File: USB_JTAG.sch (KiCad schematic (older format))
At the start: 29 parts, among them J4 USB_B_Micro, J5 AVR-JTAG-10, U10 FT2232H, U11 5M1270ZT144C5N, U12 93LCxxBxxOT, U9 TPD2EUSB30

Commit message: Updated BOM
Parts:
- removed U10: FT2232H, Package_QFP:LQFP-64_10x10mm_P0.5mm, symbol Interface_USB:FT2232H
- added U8: FT2232H, Package_QFP:TQFP-64_10x10mm_P0.5mm, symbol Interface_USB:FT2232H
- C16, C18: MFR KEMET -> Taiyo Yuden; MPN C0805C104K4RACTU -> JMK107BB7475KA-T; SPN 80-C0805C104K4R -> (none)
- C17, C19, C23, C24, C25, C26, C27, C28, C29, C30: MFR KEMET -> Taiyo Yuden; MPN C0805C104K4RACTU -> TMK107BJ104KA-T; SPN 80-C0805C104K4R -> (none)
- D1: MFR (none) -> Lite-On; MPN (none) -> LTST-C190KGKT; SPR (none) -> Mouser
- L1, L2: MFR (none) -> TDK; MPN (none) -> MMZ1608R601ATA00; SPR (none) -> Mouser
- R5: MFR (none) -> Yageo; MPN (none) -> RC0603JR-0712KL; SPR (none) -> Mouser
- R6: MFR (none) -> Yageo; MPN (none) -> RC0603JR-071KL; SPR (none) -> Mouser
- R7: MFR (none) -> Yageo; MPN (none) -> RC0603JR-071ML; SPR (none) -> Mouser
- R8: MFR (none) -> Yageo; MPN (none) -> RC0603JR-07220RL; SPR (none) -> Mouser
- R9: MFR (none) -> Yageo; MPN (none) -> RC0603JR-072K2L; SPR (none) -> Mouser
- RN2: MFR (none) -> Panasonic; MPN (none) -> EXB-38V220JV; SPR (none) -> Mouser
- RN3, RN4: MFR (none) -> Panasonic; MPN (none) -> EXB-38V103JV; SPR (none) -> Mouser
- U11: MFR (none) -> Intel; MPN (none) -> 5M1270ZT144C5N; Manufacturer_Name Intel -> (none); SPR (none) -> Mouser
- U12: value 93LCxxBxxOT -> 93LC46BT-I/OT; MFR (none) -> Microchip; MPN (none) -> 93LC46BT-I/OT; SPR (none) -> Mouser
- U9: MFR (none) -> Texas Instruments; MPN (none) -> TPD2EUSB30DRTR; SPR (none) -> Mouser
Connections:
- wire segments 141 -> 142
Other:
- moved on the sheet: D1, R8

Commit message: updated descriptions and part #'s
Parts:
- C16, C18: Description (none) -> Multilayer Ceramic Capacitors MLCC - SMD/SMT 4.7uF 6.3V X7R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; SPN (none) -> 963-JMK107BB7475KA-T; SPURL https://www.mouser.com/ProductDetail/KEMET/C0805C104K4RACTU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 -> https://www.mouser.com/ProductDetail/963-JMK107BB7475KA-T
- C17, C19, C23, C24, C25, C26, C27, C28, C29, C30: Description (none) -> Multilayer Ceramic Capacitors MLCC - SMD/SMT 0.1uF 25V X5R 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; SPN (none) -> 963-TMK107BJ104KA-T; SPURL https://www.mouser.com/ProductDetail/KEMET/C0805C104K4RACTU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 -> https://www.mouser.com/ProductDetail/963-TMK107BJ104KA-T
- D1: Description (none) -> Standard LEDs - SMD Green Clear 571nm; SPN (none) -> 859-LTST-C190KGKT; SPURL (none) -> https://www.mouser.com/ProductDetail/859-LTST-C190KGKT
- L1, L2: Description (none) -> Ferrite Beads 600 OHM 25%; SPN (none) -> 810-MMZ1608R601ATA00; SPURL (none) -> https://www.mouser.com/ProductDetail/810-MMZ1608R601ATA00
- R5: Description (none) -> Thick Film Resistors - SMD 12K OHM 5%; SPN (none) -> 603-RC0603JR-0712KL; SPURL (none) -> https://www.mouser.com/ProductDetail/603-RC0603JR-0712KL
- R6: Description (none) -> Thick Film Resistors - SMD 1K OHM 5%; SPN (none) -> 603-RC0603JR-071KL; SPURL (none) -> https://www.mouser.com/ProductDetail/603-RC0603JR-071KL
- R7: Description (none) -> Thick Film Resistors - SMD 1M OHM 5%; SPN (none) -> 603-RC0603JR-071ML; SPURL (none) -> https://www.mouser.com/ProductDetail/603-RC0603JR-071ML
- R8: Description (none) -> Thick Film Resistors - SMD 220 OHM 5%; SPN (none) -> 603-RC0603JR-07220RL; SPURL (none) -> https://www.mouser.com/ProductDetail/603-RC0603JR-07220RL
- R9: Description (none) -> Thick Film Resistors - SMD 2.2K OHM 5%; SPN (none) -> 603-RC0603JR-072K2L; SPURL (none) -> https://www.mouser.com/ProductDetail/603-RC0603JR-072K2L
- RN2: Description (none) -> Resistor Networks & Arrays 22 OHM 5%; SPN (none) -> 667-EXB-38V220JV; SPURL (none) -> https://www.mouser.com/ProductDetail/667-EXB-38V220JV
- RN3, RN4: Description (none) -> Resistor Networks & Arrays 10K OHM 5%; SPN (none) -> 667-EXB-38V103JV; SPURL (none) -> https://www.mouser.com/ProductDetail/667-EXB-38V103JV
- U11: SPN (none) -> 989-5M1270ZT144C5N; SPURL (none) -> https://www.mouser.com/ProductDetail/989-5M1270ZT144C5N
- U12: Description (none) -> EEPROM 64x16; SPN (none) -> 579-93LC46BT-I/OT; SPURL (none) -> https://www.mouser.com/ProductDetail/579-93LC46BT-I/OT
- U8: symbol Interface_USB:FT2232H -> rc2014_max_v-rescue:FT2232H-Interface_USB; Description (none) -> USB Interface IC USB HS to Dual UART/ FIFO/SPI/JTAG/I2C; SPN (none) -> 895-FT2232HL; SPURL (none) -> https://www.mouser.com/ProductDetail/895-FT2232HL
- U9: Description (none) -> ESD Suppressors / TVS Diodes 2Ch ESD Solution; SPN (none) -> 595-TPD2EUSB30DRTR; SPURL (none) -> https://www.mouser.com/ProductDetail/595-TPD2EUSB30DRTR

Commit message: mirror flipped the chips
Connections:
- net JTAG_TDO: now also RN3.2 (R2.1); no longer RN3.3 (R3.1)
- net JTAG_TMS: now also RN3.3 (R3.1); no longer RN3.2 (R2.1)
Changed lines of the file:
@@
 	7930 2430 8060 2430
 Wire Wire Line
-	9890 3780 10300 3780
-Wire Wire Line
 	10450 3780 10450 3790
 Wire Wire Line
-	9890 3680 10200 3680
-Wire Wire Line
 	10450 3680 10450 3690
-Wire Wire Line
-	9890 3580 10100 3580
-Wire Wire Line
-	9890 3480 10000 3480
-Wire Wire Line
-	10000 3000 10000 3480
-Wire Wire Line
-	10000 3480 10450 3480
-Wire Wire Line
-	10100 3000 10100 3580
-Wire Wire Line
-	10100 3580 10450 3580
-Wire Wire Line
-	10200 3000 10200 3680
-Wire Wire Line
-	10200 3680 10450 3680
-Wire Wire Line
-	10300 3000 10300 3780
-Wire Wire Line
-	10300 3780 10450 3780
 Wire Wire Line
 	10300 2600 10300 2610
@@
 Connection ~ 1640 6910
 Connection ~ 1640 7210
-Connection ~ 10000 3480
-Connection ~ 10100 3580
-Connection ~ 10200 3680
-Connection ~ 10300 3780
 Connection ~ 6550 1830
 Connection ~ 3480 3830
@@
 NoConn ~ 7400 5330
 NoConn ~ 5000 5630
+Wire Wire Line
+	9890 3680 10100 3680
+Wire Wire Line
+	9890 3580 10200 3580
+Wire Wire Line
+	10200 3000 10200 3580
+Connection ~ 10200 3580
+Wire Wire Line
+	10200 3580 10450 3580
+Wire Wire Line
+	10100 3000 10100 3680
+Connection ~ 10100 3680
+Wire Wire Line
+	10100 3680 10450 3680
+Wire Wire Line
+	9890 3780 10300 3780
+Wire Wire Line
+	9890 3480 10000 3480
+Wire Wire Line
+	10000 3000 10000 3480
+Connection ~ 10000 3480
+Wire Wire Line
+	10000 3480 10450 3480
+Wire Wire Line
+	10300 3000 10300 3780
+Connection ~ 10300 3780
+Wire Wire Line
+	10300 3780 10450 3780
 $EndSCHEMATC

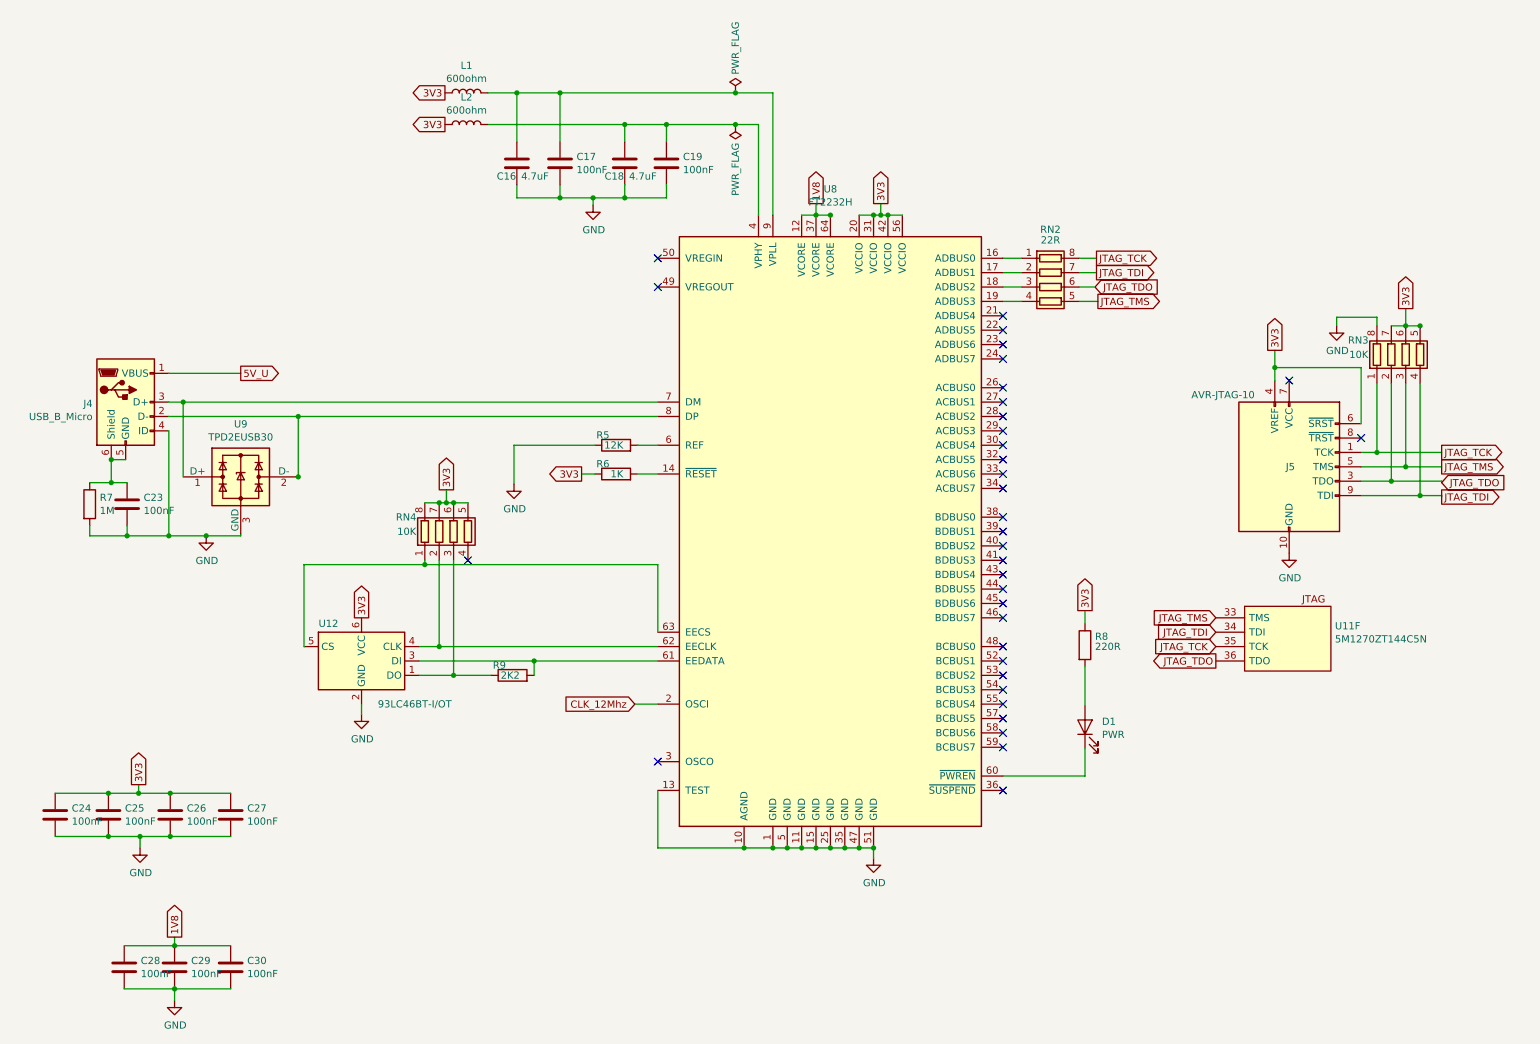
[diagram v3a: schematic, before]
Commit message: moved things around to improve routing, fixed power plane
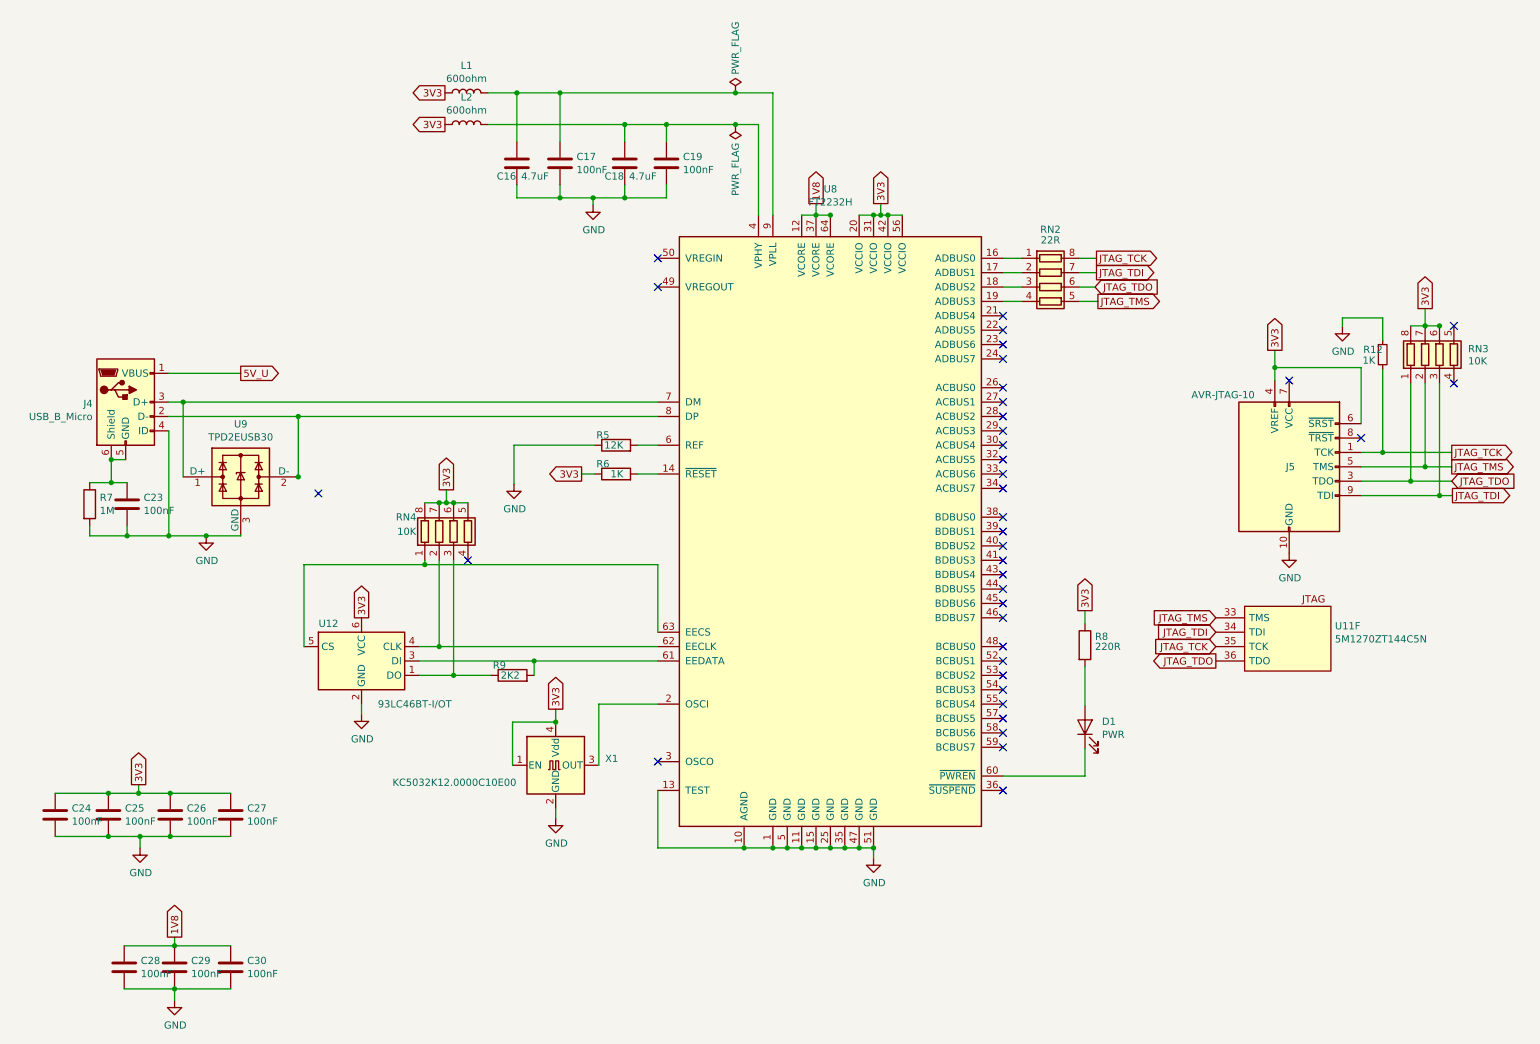
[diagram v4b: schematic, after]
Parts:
- added R12: 1K, Resistor_SMD:R_0603_1608Metric_Pad1.05x0.95mm_HandSolder, symbol Device:R_Small
- added X1: KC5032K12.0000C10E00, Oscillator:Oscillator_SMD_Fordahl_DFAS15-4Pin_5.0x3.2mm_HandSoldering, symbol Oscillator:KC5032K12.0000C10E00
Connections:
- net 3V3: now also RN3.8 (R1.2), X1.1 (EN), X1.4 (Vdd); no longer RN3.5 (R4.2)
- net GND: now also R12.1, X1.2 (GND); no longer RN3.8 (R1.2)
- net JTAG_TCK: now also R12.2; no longer RN3.1 (R1.1)
- net JTAG_TDI: now also RN3.3 (R3.1); no longer RN3.4 (R4.1)
- net JTAG_TDO: now also RN3.1 (R1.1); no longer RN3.2 (R2.1)
- net JTAG_TMS: now also RN3.2 (R2.1); no longer RN3.3 (R3.1)
- net CLK_12Mhz: no longer names the net of U8.2 (OSCI)
- net CLK_12Mhz: now also X1.3 (OUT)
- no-connect marks 35 -> 38
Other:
- moved on the sheet: RN3
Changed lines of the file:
@@
-$EndComp
-$Comp
-L Device:R_Pack04 RN3
-U 1 1 5CF8ACD2
-P 10200 2800
-AR Path="/5D0F9837/5CF8ACD2" Ref="RN3"  Part="1"
-AR Path="/5CF8ACD2" Ref="RN?"  Part="1"
-AR Path="/5CFABACD/5CF8ACD2" Ref="RN?"  Part="1"
-F 0 "RN3" H 9870 2900 50  0000 C CNN
-F 1 "10K" H 9874 2800 50  0000 C CNN
-F 2 "Resistor_SMD:R_Array_Concave_4x0603" V 10475 2800 50  0001 C CNN
-F 3 "https://www.mouser.com/datasheet/2/315/AOC0000C14-1108062.pdf" H 10200 2800 50  0001 C CNN
-F 4 "Resistor Networks & Arrays 10K OHM 5%" H 9870 3000 50  0001 C CNN "Description"
-F 5 "Panasonic" H 10200 2800 50  0001 C CNN "MFR"
-F 6 "EXB-38V103JV" H 10200 2800 50  0001 C CNN "MPN"
-F 7 "667-EXB-38V103JV" H 9870 3000 50  0001 C CNN "SPN"
-F 8 "Mouser" H 10200 2800 50  0001 C CNN "SPR"
-F 9 "https://www.mouser.com/ProductDetail/667-EXB-38V103JV" H 9870 3000 50  0001 C CNN "SPURL"
-	1    10200 2800
-	1    0    0    -1
 $EndComp
 $Comp
 L power:GND #PWR?
 U 1 1 5D1A4182
-P 9720 2600
+P 9760 2605
 AR Path="/5D1A4182" Ref="#PWR?"  Part="1"
 AR Path="/5CB63856/5D1A4182" Ref="#PWR?"  Part="1"
@@
 AR Path="/5CFABACD/5D1A4182" Ref="#PWR?"  Part="1"
 AR Path="/5D0F9837/5D1A4182" Ref="#PWR041"  Part="1"
-F 0 "#PWR041" H 9720 2350 50  0001 C CNN
-F 1 "GND" H 9725 2427 50  0000 C CNN
-F 2 "" H 9720 2600 50  0001 C CNN
-F 3 "" H 9720 2600 50  0001 C CNN
-	1    9720 2600
+F 0 "#PWR041" H 9760 2355 50  0001 C CNN
+F 1 "GND" H 9765 2432 50  0000 C CNN
+F 2 "" H 9760 2605 50  0001 C CNN
+F 3 "" H 9760 2605 50  0001 C CNN
+	1    9760 2605
 	1    0    0    -1
 $EndComp
@@
 Text GLabel 8060 2430 2    50   Output ~ 0
 JTAG_TMS
-Text GLabel 10450 3790 2    50   Output ~ 0
+Text GLabel 10525 3780 2    50   Output ~ 0
 JTAG_TDI
-Text GLabel 10450 3690 2    50   Input ~ 0
+Text GLabel 10520 3680 2    50   Input ~ 0
 JTAG_TDO
-Text GLabel 10450 3580 2    50   Output ~ 0
+Text GLabel 10520 3580 2    50   Output ~ 0
 JTAG_TMS
-Text GLabel 10450 3480 2    50   Output ~ 0
+Text GLabel 10520 3480 2    50   Output ~ 0
 JTAG_TCK
 Text GLabel 8880 4730 0    50   Input ~ 0
@@
 Text GLabel 8880 4830 0    50   Input ~ 0
 JTAG_TCK
-Text GLabel 4840 5230 0    50   Input ~ 0
-CLK_12Mhz
 Text GLabel 2100 2930 2    50   Output ~ 0
 5V_U
@@
 Text GLabel 3530 3740 1    50   Output ~ 0
 3V3
-Text GLabel 10200 2480 1    50   Output ~ 0
+Text GLabel 10335 2480 1    50   Output ~ 0
 3V3
 Text GLabel 9290 2770 1    50   Output ~ 0
@@
 	7930 2430 8060 2430
 Wire Wire Line
-	10450 3780 10450 3790
-Wire Wire Line
-	10450 3680 10450 3690
-Wire Wire Line
-	10300 2600 10300 2610
-Wire Wire Line
-	10200 2480 10200 2600
+	10435 2600 10435 2610
+Wire Wire Line
+	10335 2480 10335 2600
 Wire Wire Line
 	3380 3830 3480 3830
@@
 	3530 3830 3580 3830
 Wire Wire Line
-	10200 2600 10300 2600
-Wire Wire Line
-	10100 2600 10200 2600
-Wire Wire Line
-	10000 2600 10000 2540
-Wire Wire Line
-	10000 2540 9720 2540
-Wire Wire Line
-	9720 2540 9720 2600
+	10335 2600 10435 2600
+Wire Wire Line
+	10235 2600 10335 2600
+Wire Wire Line
+	10040 2545 9760 2545
+Wire Wire Line
+	9760 2545 9760 2605
 Wire Wire Line
 	9890 3280 9890 2890
@@
 Wire Wire Line
 	1640 7210 2030 7210
-Wire Wire Line
-	4840 5230 5000 5230
 Wire Wire Line
 	7400 5730 7970 5730
@@
 Connection ~ 3580 3830
 Connection ~ 3530 3830
-Connection ~ 10200 2600
-Connection ~ 10300 2600
+Connection ~ 10335 2600
 Connection ~ 9290 2890
 Connection ~ 1400 6150
@@
 NoConn ~ 7400 5330
 NoConn ~ 5000 5630
-Wire Wire Line
-	9890 3680 10100 3680
-Wire Wire Line
-	9890 3580 10200 3580
-Wire Wire Line
-	10200 3000 10200 3580
-Connection ~ 10200 3580
-Wire Wire Line
-	10200 3580 10450 3580
-Wire Wire Line
-	10100 3000 10100 3680
-Connection ~ 10100 3680
-Wire Wire Line
-	10100 3680 10450 3680
-Wire Wire Line
-	9890 3780 10300 3780
-Wire Wire Line
-	9890 3480 10000 3480
-Wire Wire Line
-	10000 3000 10000 3480
-Connection ~ 10000 3480
-Wire Wire Line
-	10000 3480 10450 3480
-Wire Wire Line
-	10300 3000 10300 3780
-Connection ~ 10300 3780
-Wire Wire Line
-	10300 3780 10450 3780
+$Comp
+L Oscillator:KC5032K12.0000C10E00 X1
+U 1 1 5D18454F
+P 4290 5655
+F 0 "X1" H 4634 5701 50  0000 L CNN
+F 1 "KC5032K12.0000C10E00" H 3155 5535 50  0000 L CNN
+F 2 "Oscillator:Oscillator_SMD_Fordahl_DFAS15-4Pin_5.0x3.2mm_HandSoldering" H 4990 5305 50  0001 C CNN
+F 3 "http://www.abracon.com/Oscillators/ASV.pdf" H 4190 5655 50  0001 C CNN
+	1    4290 5655
+	1    0    0    -1
+$EndComp
+Wire Wire Line
+	4590 5655 4590 5230
+Wire Wire Line
+	4590 5230 5000 5230
+Wire Wire Line
+	3990 5655 3990 5355
+Wire Wire Line
+	3990 5355 4290 5355
+Text GLabel 4290 5265 1    50   Output ~ 0
+3V3
+Wire Wire Line
+	4290 5265 4290 5355
+Connection ~ 4290 5355
+$Comp
+L power:GND #PWR02
+U 1 1 5D1A3145
+P 4290 6025
+F 0 "#PWR02" H 4290 5775 50  0001 C CNN
+F 1 "GND" H 4295 5852 50  0000 C CNN
+F 2 "" H 4290 6025 50  0001 C CNN
+F 3 "" H 4290 6025 50  0001 C CNN
+	1    4290 6025
+	1    0    0    -1
+$EndComp
+Wire Wire Line
+	4290 5955 4290 6025
+NoConn ~ 2640 3765
+Connection ~ 10435 2600
+Wire Wire Line
+	10435 3000 10435 3780
+$Comp
+L Device:R_Pack04 RN3
+U 1 1 5CF8ACD2
+P 10435 2800
+AR Path="/5D0F9837/5CF8ACD2" Ref="RN3"  Part="1"
+AR Path="/5CF8ACD2" Ref="RN?"  Part="1"
+AR Path="/5CFABACD/5CF8ACD2" Ref="RN?"  Part="1"
+F 0 "RN3" H 10705 2840 50  0000 C CNN
+F 1 "10K" H 10700 2755 50  0000 C CNN
+F 2 "Resistor_SMD:R_Array_Concave_4x0603" V 10710 2800 50  0001 C CNN
+F 3 "https://www.mouser.com/datasheet/2/315/AOC0000C14-1108062.pdf" H 10435 2800 50  0001 C CNN
+F 4 "Resistor Networks & Arrays 10K OHM 5%" H 10105 3000 50  0001 C CNN "Description"
+F 5 "Panasonic" H 10435 2800 50  0001 C CNN "MFR"
+F 6 "EXB-38V103JV" H 10435 2800 50  0001 C CNN "MPN"
+F 7 "667-EXB-38V103JV" H 10105 3000 50  0001 C CNN "SPN"
+F 8 "Mouser" H 10435 2800 50  0001 C CNN "SPR"
+F 9 "https://www.mouser.com/ProductDetail/667-EXB-38V103JV" H 10105 3000 50  0001 C CNN "SPURL"
+	1    10435 2800
+	1    0    0    -1
+$EndComp
+Wire Wire Line
+	9890 3780 10435 3780
+Connection ~ 10435 3780
+Wire Wire Line
+	10435 3780 10525 3780
+Wire Wire Line
+	9890 3480 10040 3480
+Connection ~ 10040 3480
+Wire Wire Line
+	10040 3480 10520 3480
+$Comp
+L Device:R_Small R12
+U 1 1 5D2F206D
+P 10040 2800
+F 0 "R12" H 9905 2835 50  0000 L CNN
+F 1 "1K" H 9900 2760 50  0000 L CNN
+F 2 "Resistor_SMD:R_0603_1608Metric_Pad1.05x0.95mm_HandSolder" H 10040 2800 50  0001 C CNN
+F 3 "~" H 10040 2800 50  0001 C CNN
+	1    10040 2800
+	1    0    0    -1
+$EndComp
+Wire Wire Line
+	10040 2545 10040 2700
+Wire Wire Line
+	10040 2900 10040 3480
+NoConn ~ 10535 3000
+NoConn ~ 10535 2600
+Wire Wire Line
+	10235 3000 10235 3680
+Wire Wire Line
+	9890 3680 10235 3680
+Connection ~ 10235 3680
+Wire Wire Line
+	10235 3680 10520 3680
+Wire Wire Line
+	10335 3000 10335 3580
+Wire Wire Line
+	9890 3580 10335 3580
+Connection ~ 10335 3580
+Wire Wire Line
+	10335 3580 10520 3580
 $EndSCHEMATC
